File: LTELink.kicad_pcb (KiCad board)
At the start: 4 copper layers, 93.3 x 65.8 mm, 95 parts, among them IC1 RTL8305NB-VC-CG, J1 DF40C100DS04V51, J2 DF40C100DS04V51, J3 DF40C100DS04V51, J4 1759547-1, J5 USB_A, J6 Conn_01x03_Pin, J7 Micro_SD_Card_Det1, J8 USB_A, J9 USB_C_Receptacle_USB2.0_16P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

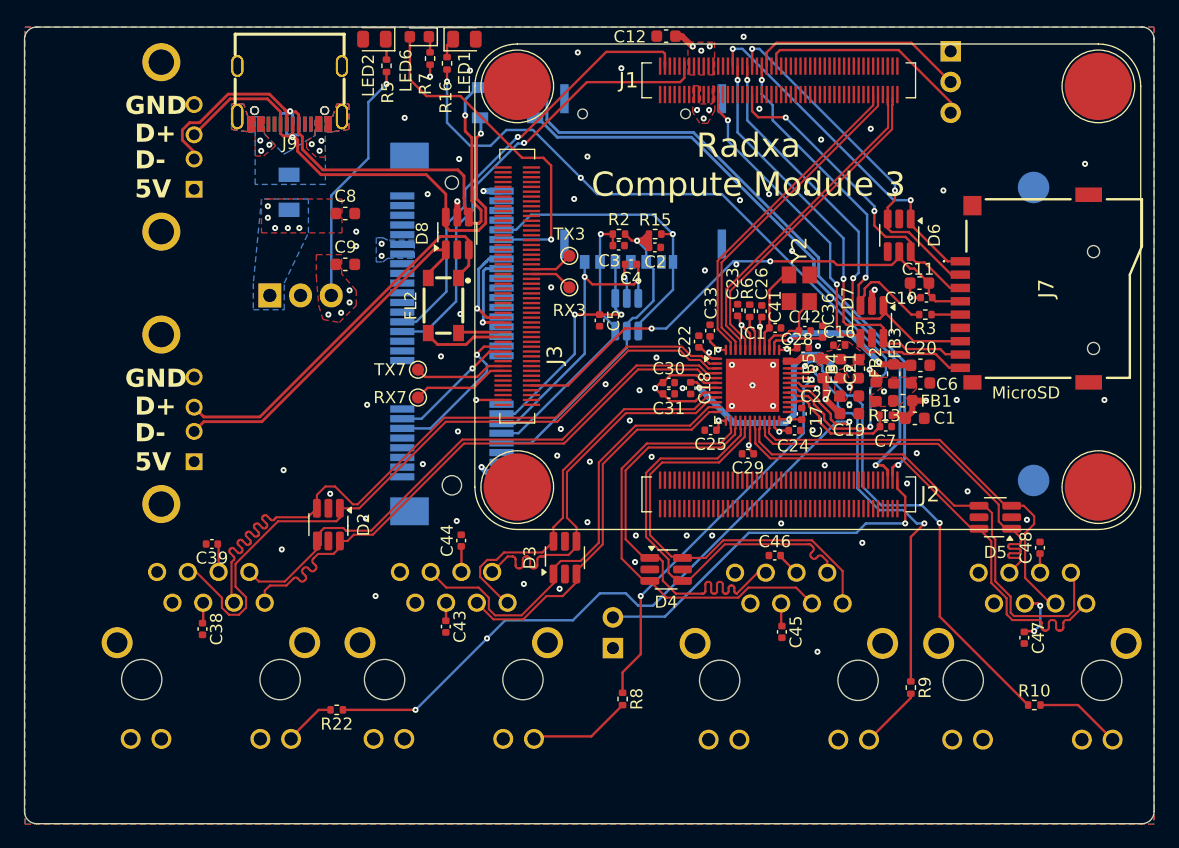
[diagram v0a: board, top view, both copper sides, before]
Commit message: replaced ferrites with 0 omh resitors, finalized standoff solution
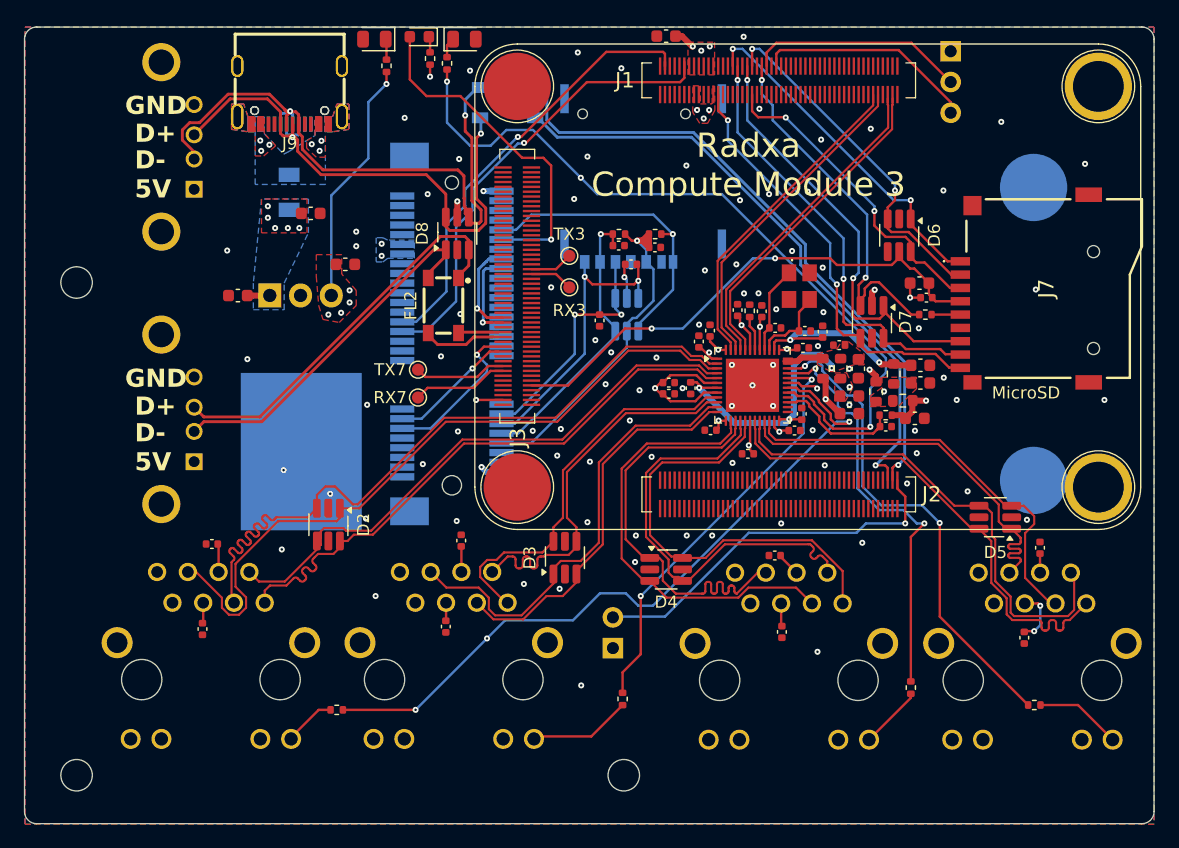
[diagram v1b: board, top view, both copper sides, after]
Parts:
- removed FB1, FB2, FB3, FB4, FB5: BLM18PG121SN1D, Inductor_SMD:L_0603_1608Metric
- added C13: 10u, Capacitor_SMD:C_0603_1608Metric, F.Cu at (165.3, 78.8)
- added R11: 0, Resistor_SMD:R_0603_1608Metric, F.Cu at (218.0, 86.7)
- added R12: 0, Resistor_SMD:R_0603_1608Metric, F.Cu at (219.5, 85.2)
- added R14: 0, Resistor_SMD:R_0603_1608Metric, F.Cu at (215.1, 84.8)
- added R19: 0, Resistor_SMD:R_0603_1608Metric, F.Cu at (213.7, 84.8)
- added R4: 0, Resistor_SMD:R_0603_1608Metric, F.Cu at (220.2, 87.5)
- J1, J2, J3: value DF40C100DS04V51 -> DF40HC(3.0)-100DS-0.4V(51)
- moved C8 2.86 mm to (171.3, 72.0)
- moved Y2 0.18 mm to (211.7, 78.0)
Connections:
- J4 pad 53: (no net) -> GND
- Raxda pad NUT: (no net) -> GND
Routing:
- net +5V: track 6.36 -> 8.23 mm
- net Net-(LED2-Pad1): track 0.65 -> 1.72 mm
- net /SD Card/SDMMC_VDD: track 43.0 -> 43.2 mm, vias 3 -> 2
- net GND: vias 71 -> 91
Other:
- outline, holes or cut-outs redrawn
- board text added: "3.3V"
- board text added: "LAN"
- board text added: "WWAN"
